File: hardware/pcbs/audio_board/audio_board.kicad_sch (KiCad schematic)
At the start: 42 parts, among them J2 Expansion, J3 AudioJack3, U11 TPS65130RGE, U12 L79L09_SOT89, U13 L78L09_SOT89, U4 MCP1700x-330xxMB, U5 AP7313-18SAG-7

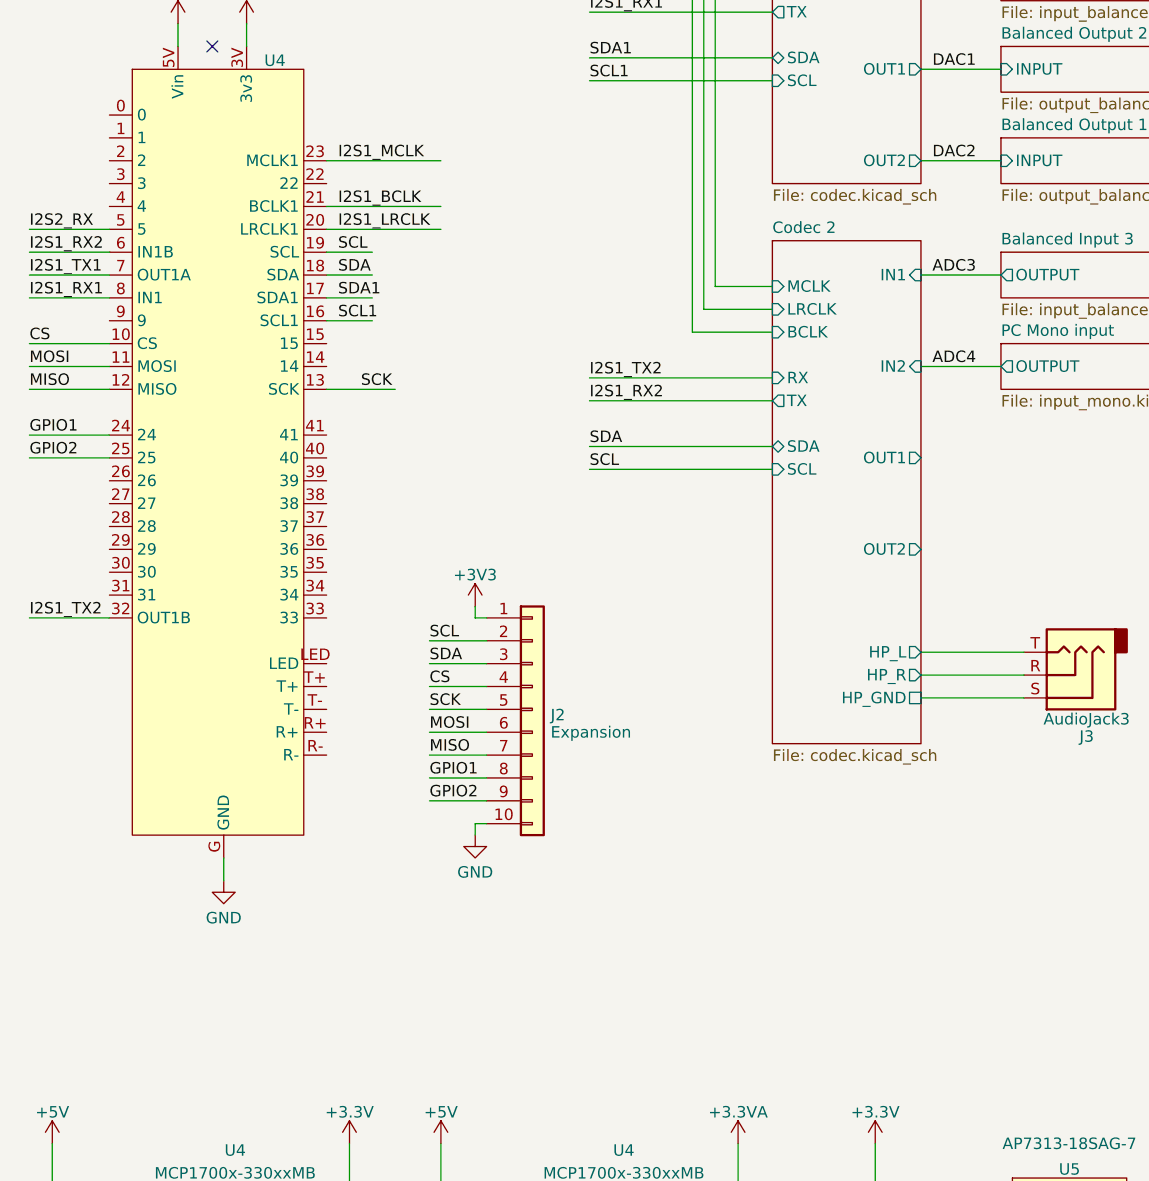
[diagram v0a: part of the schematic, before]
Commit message: Small audio board fixes and add DHAN-M module
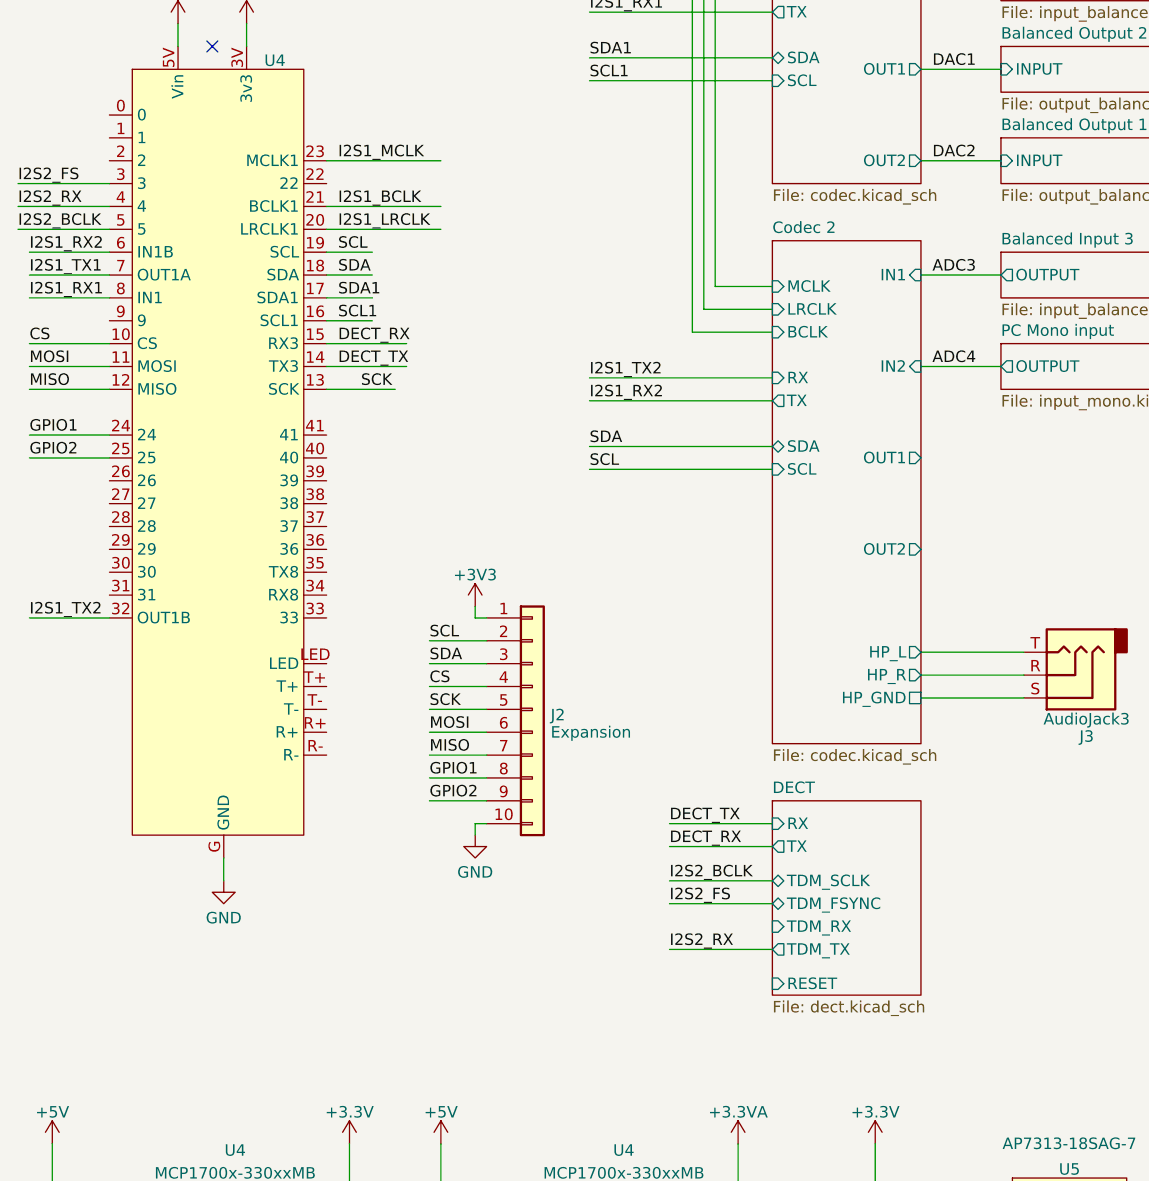
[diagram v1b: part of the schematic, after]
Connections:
- net I2S2_RX: now also U4.4; no longer U4.5
- net DECT_TX: now reaches U4.14
- net DECT_RX: now reaches U4.15
- net I2S2_FS: now reaches U4.3
- new net I2S2_BCLK: U4.5
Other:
- added sheet DECT (dect.kicad_sch)

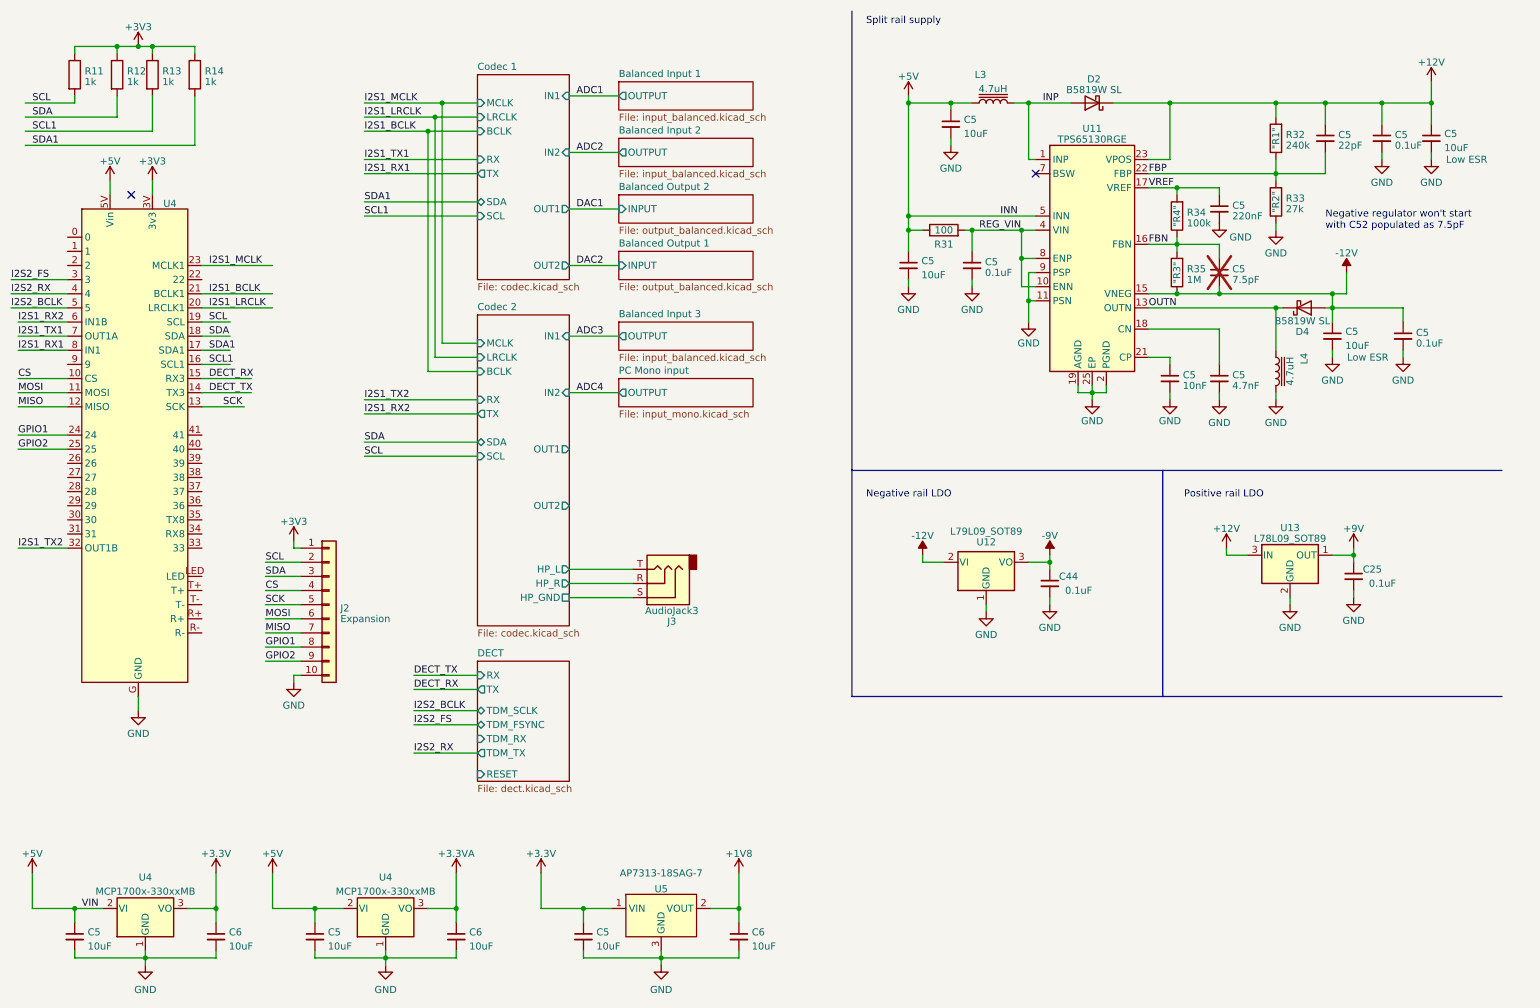
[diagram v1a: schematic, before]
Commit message: Redo layout for the audio board
* Height of the board decreased by 2cm
* Switching regulator removed
* Switched balanced audio I/O for single-rail versions
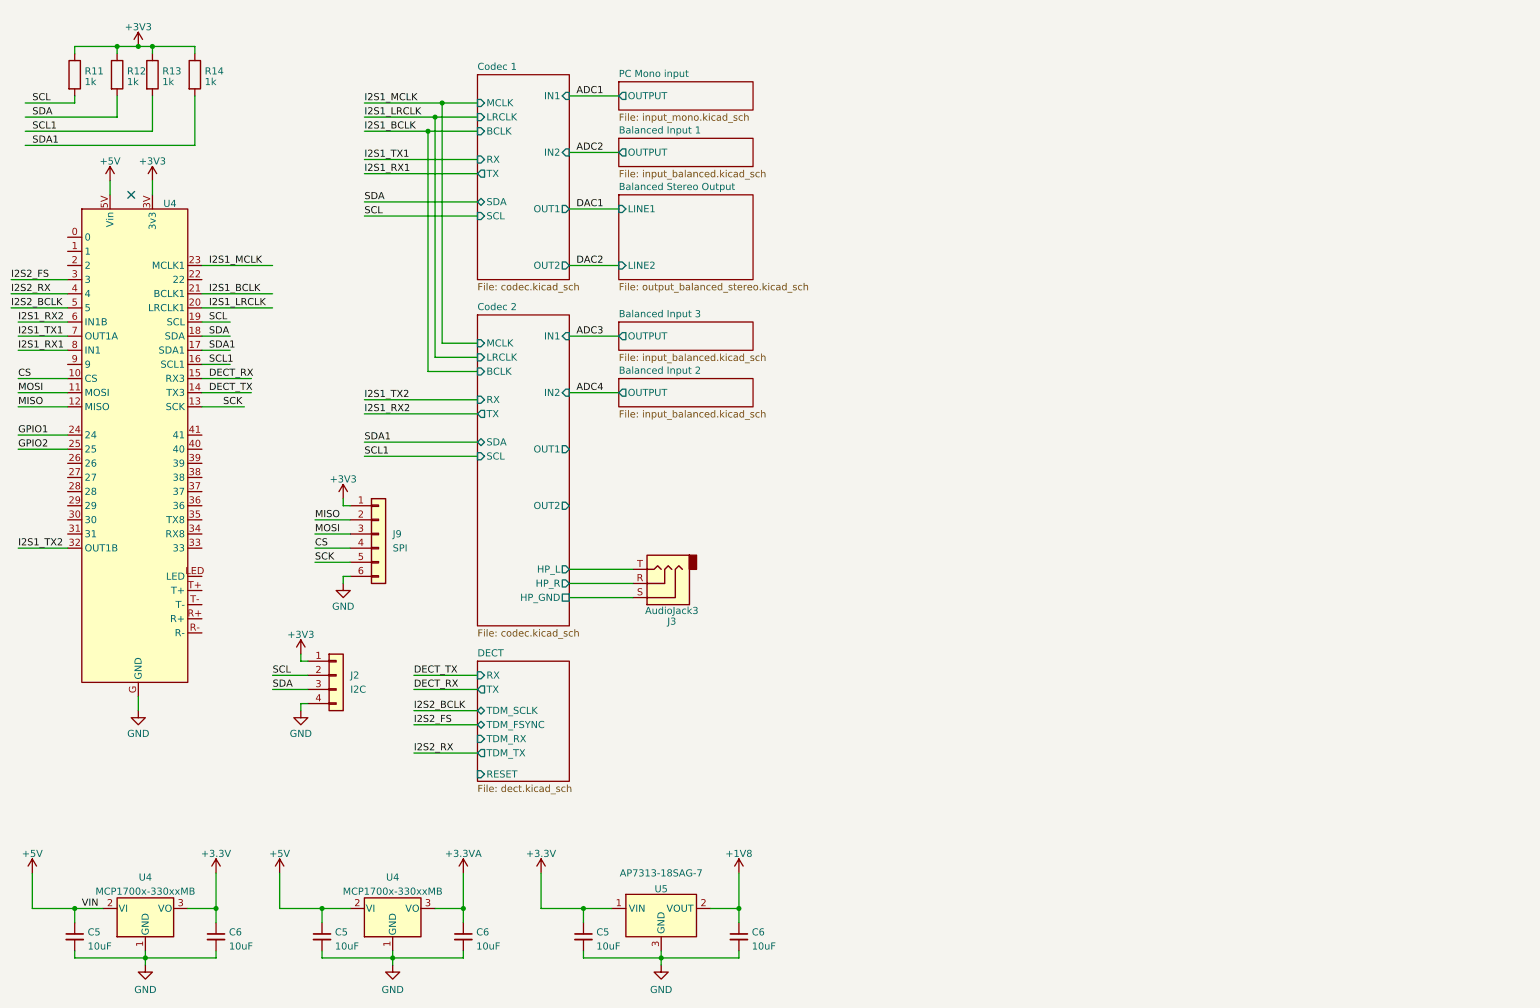
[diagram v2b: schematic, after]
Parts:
- removed C25, C44, C5 (x3): 0.1uF, Capacitor_SMD:C_0603_1608Metric_Pad1.08x0.95mm_HandSolder, symbol Device:C_Small
- removed C5: 22pF, Capacitor_SMD:C_0603_1608Metric_Pad1.08x0.95mm_HandSolder, symbol Device:C_Small
- removed C5 (x4): 10uF, Capacitor_SMD:C_0805_2012Metric_Pad1.18x1.45mm_HandSolder, symbol Device:C_Small
- removed C5: 220nF, Capacitor_SMD:C_0603_1608Metric_Pad1.08x0.95mm_HandSolder, symbol Device:C_Small
- removed C5: 4.7nF, Capacitor_SMD:C_0603_1608Metric_Pad1.08x0.95mm_HandSolder, symbol Device:C_Small
- removed C5: 10nF, Capacitor_SMD:C_0603_1608Metric_Pad1.08x0.95mm_HandSolder, symbol Device:C_Small
- removed C5: 7.5pF, Capacitor_SMD:C_0603_1608Metric_Pad1.08x0.95mm_HandSolder, symbol Device:C_Small
- removed D2, D4: B5819W SL, Diode_SMD:D_SOD-123, symbol Device:D_Schottky
- removed J2: Expansion, Connector_PinHeader_2.54mm:PinHeader_1x10_P2.54mm_Vertical, symbol Connector_Generic:Conn_01x10
- removed L3, L4: 4.7uH, Inductor_SMD:L_Sunlord_SWPA4030S, symbol Device:L_Iron
- removed R31: 100, Resistor_SMD:R_0603_1608Metric_Pad0.98x0.95mm_HandSolder, symbol Device:R
- removed R32: 240k, Resistor_SMD:R_0603_1608Metric_Pad0.98x0.95mm_HandSolder, symbol Device:R
- removed R33: 27k, Resistor_SMD:R_0603_1608Metric_Pad0.98x0.95mm_HandSolder, symbol Device:R
- removed R34: 100k, Resistor_SMD:R_0603_1608Metric_Pad0.98x0.95mm_HandSolder, symbol Device:R
- removed R35: 1M, Resistor_SMD:R_0603_1608Metric_Pad0.98x0.95mm_HandSolder, symbol Device:R
- removed U11: TPS65130RGE, Package_DFN_QFN:VQFN-24-1EP_4x4mm_P0.5mm_EP2.45x2.45mm_ThermalVias, symbol Regulator_Switching:TPS65130RGE
- removed U12: L79L09_SOT89, Package_TO_SOT_SMD:SOT-89-3, symbol Regulator_Linear:L79L05_SOT89
- removed U13: L78L09_SOT89, Package_TO_SOT_SMD:SOT-89-3, symbol Regulator_Linear:L78L09_SOT89
- added J2: I2C, Connector_PinHeader_2.54mm:PinHeader_1x04_P2.54mm_Vertical, symbol Connector_Generic:Conn_01x04
- added J9: SPI, Connector_PinHeader_2.54mm:PinHeader_1x06_P2.54mm_Vertical, symbol Connector_Generic:Conn_01x06
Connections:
- net +3V3: now also J2.1 (Pin_1), J9.1 (Pin_1)
- net CS: now also J9.4 (Pin_4)
- net GND: now also J2.4 (Pin_4), J9.6 (Pin_6)
- net MISO: now also J9.2 (Pin_2)
- net MOSI: now also J9.3 (Pin_3)
- net SCK: now also J9.5 (Pin_5)
- net SCL: now also J2.2 (Pin_2)
- net SDA: now also J2.3 (Pin_3)
- no-connect marks 2 -> 1
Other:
- removed sheet Balanced Output 1
- removed sheet Balanced Output 2
- added sheet Balanced Stereo Output (output_balanced_stereo.kicad_sch)
- note removed: "Negative rail LDO"
- note removed: "Negative regulator won't start with C52 populated as 7.5pF"
- note removed: "Positive rail LDO"
- note removed: "Split rail supply"
- moved on the sheet: C5, C6, U4

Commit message: audio_board: Rework for DECT plug-in module
Redesigned the DECT area to accept a daughterboard with whatever DECT
module ends up working. Added more holes and silkscreen to make the
board neater.
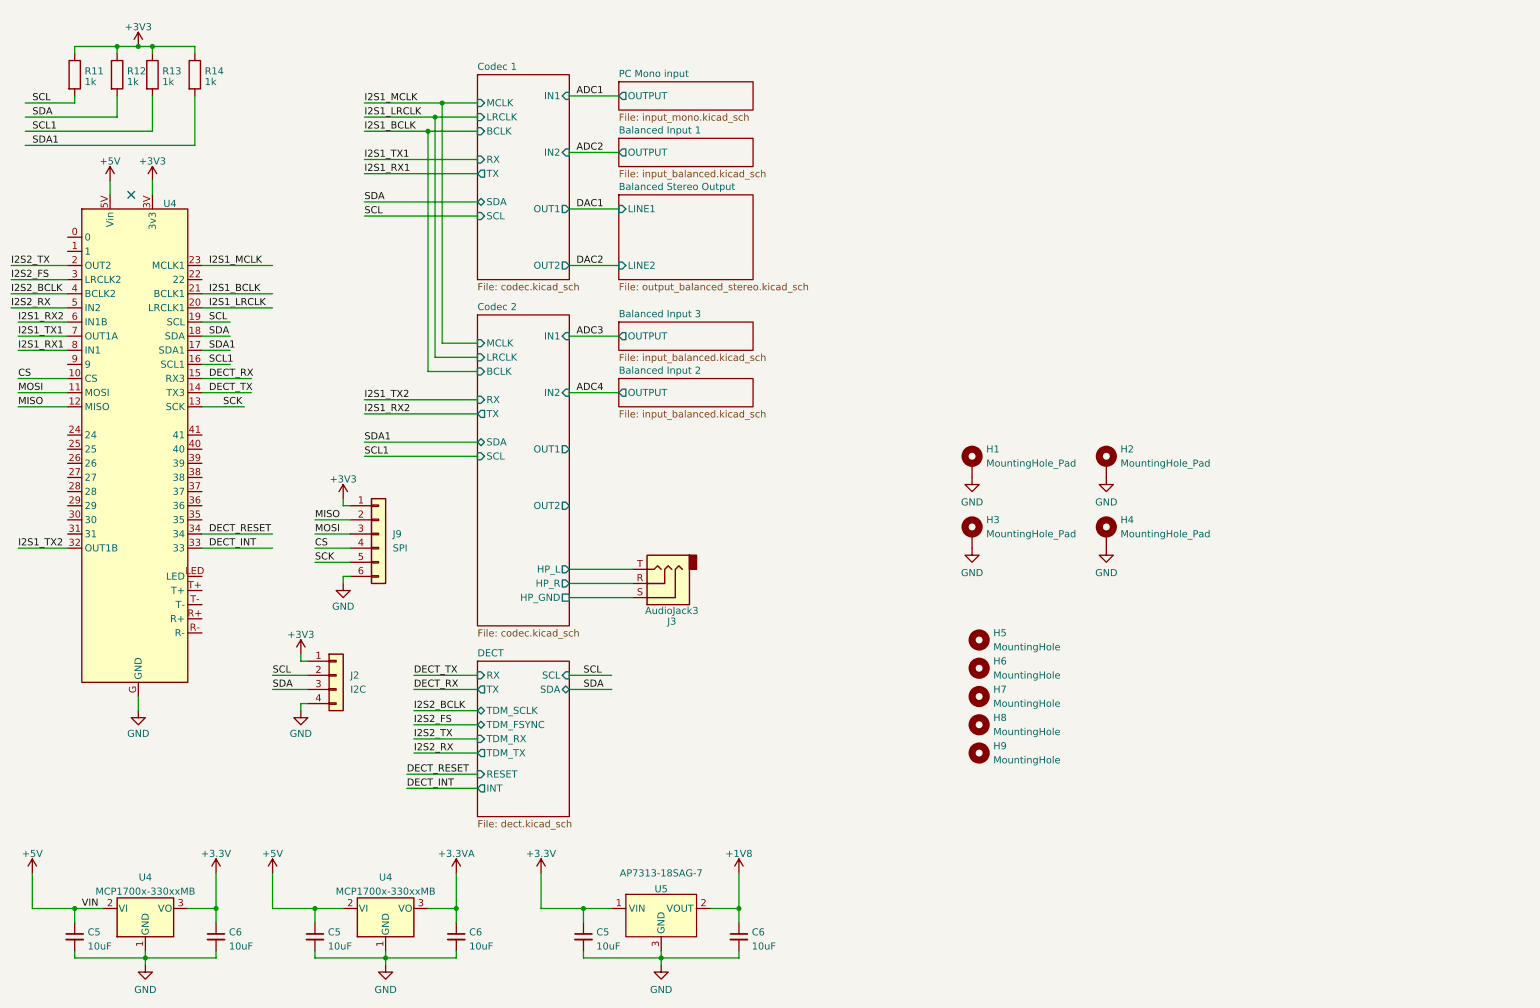
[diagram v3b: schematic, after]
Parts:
- added H1, H2, H3, H4: MountingHole_Pad, MountingHole:MountingHole_3.2mm_M3_Pad_Via, symbol Mechanical:MountingHole_Pad
- added H5, H6, H7, H8, H9: MountingHole, MountingHole:MountingHole_3.2mm_M3_DIN965, symbol Mechanical:MountingHole
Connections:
- net GND: now also H1.1, H2.1, H3.1, H4.1
- net I2S2_BCLK: now also U4.4; no longer U4.5
- net I2S2_RX: now also U4.5; no longer U4.4
- net I2S2_TX: now reaches U4.2
- net DECT_INT: now reaches U4.33
- net DECT_RESET: now reaches U4.34
- net GPIO1: no longer names the net of U4.24
- net GPIO2: no longer names the net of U4.25
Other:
- sheet DECT ports: added INT, SCL, SDA; removed none
- moved on the sheet: C5, C6, U4
